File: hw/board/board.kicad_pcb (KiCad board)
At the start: 4 copper layers, 100 x 85 mm, 78 parts, among them J1 Conn_ARM_JTAG_SWD_10, J2 Conn_ARM_JTAG_SWD_10, SW1 TSB008A2526A, SW2 TSB008A2526A, U1 STM32F302CBTx, U2 W25Q128JVSIQTR, U3 AP7361C-18SP-13, U4 AP7361C-10E, U5 TPS54331DR, U6 XC7A35T-FTG256

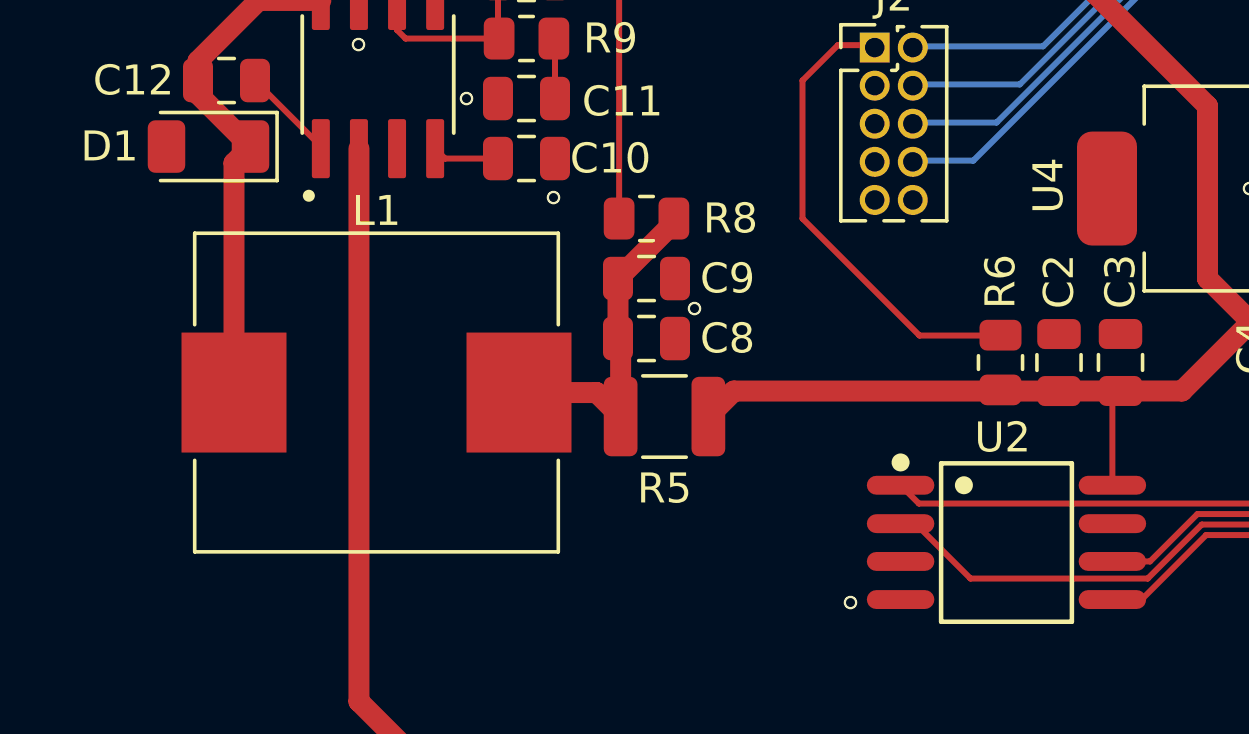
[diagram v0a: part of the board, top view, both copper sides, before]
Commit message: Replaced inductor footprint
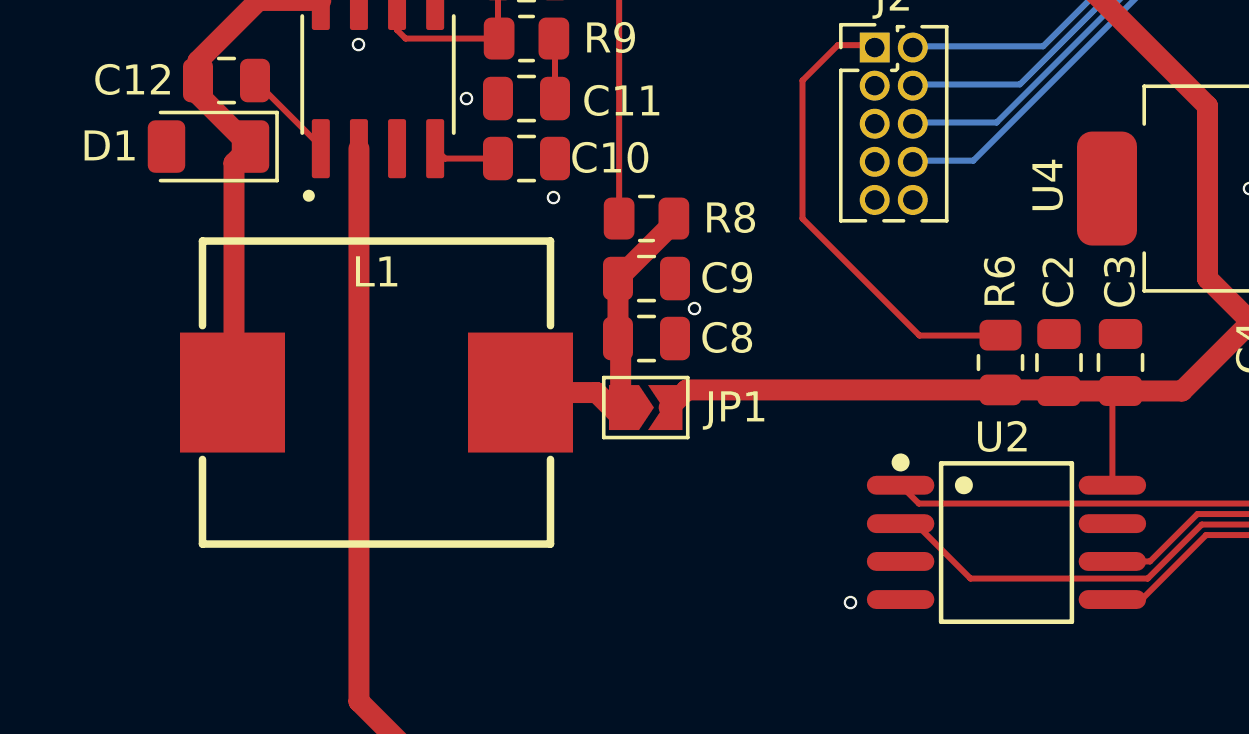
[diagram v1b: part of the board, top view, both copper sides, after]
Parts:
- removed R5: 0, Resistor_SMD:R_1210_3225Metric
- added JP1: SolderJumper_2_Open, Jumper:SolderJumper-2_P1.3mm_Open_TrianglePad1.0x1.5mm, F.Cu at (111.0, 95.5)
- L1: footprint Inductor_SMD:L_Chilisin_BMRF00101040 -> EasyEDA:IND-SMD_L11.6-W10.1
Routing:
- net +2V5: track 241.6 -> 242.8 mm

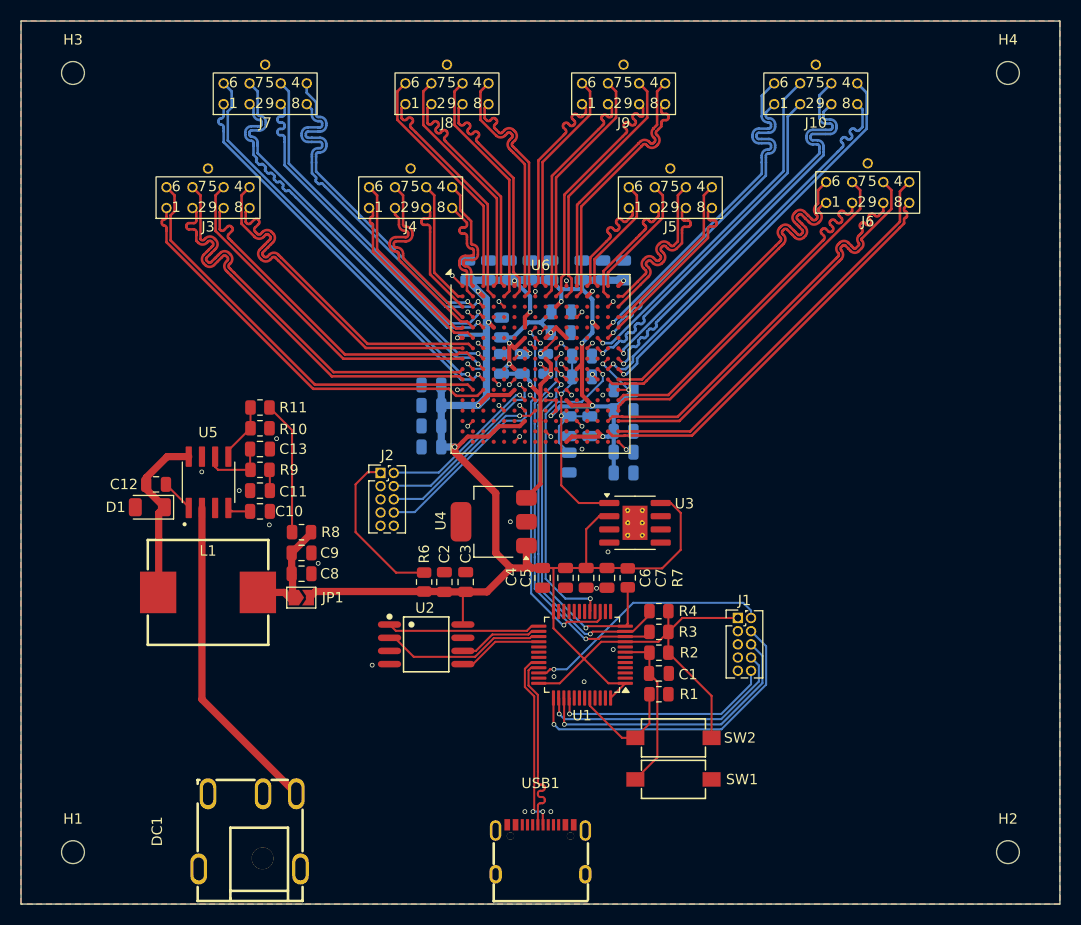
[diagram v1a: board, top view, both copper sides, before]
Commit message: Updated silkscreen
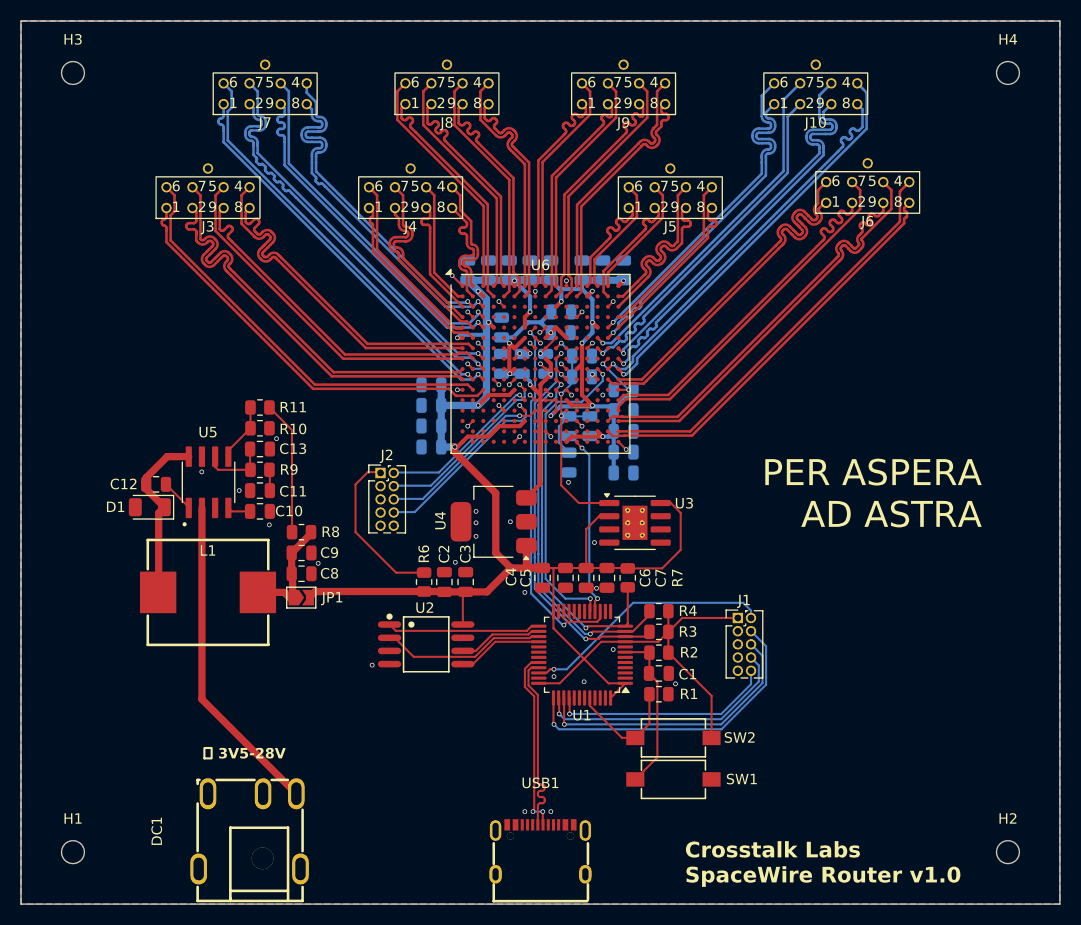
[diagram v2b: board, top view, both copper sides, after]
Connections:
- U1 pad 16: unconnected-(U1-PA6-Pad16) -> DOUT
- U6 pad L15: unconnected-(U6A-IO_L3P_T0_DQS_PUDC_B_14-PadL15) -> GND
- U6 pad T12: unconnected-(U6A-IO_L15N_T2_DQS_DOUT_CSO_B_14-PadT12) -> DOUT
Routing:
- net DOUT: track 0.00 -> 17.3 mm, vias 0 -> 2
- net GND: vias 45 -> 51
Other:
- board text added: "Crosstalk Labs SpaceWire Router v1.0"
- board text added: "PER ASPERA AD ASTRA"
- board text added: "⎓ 3V5-28V"

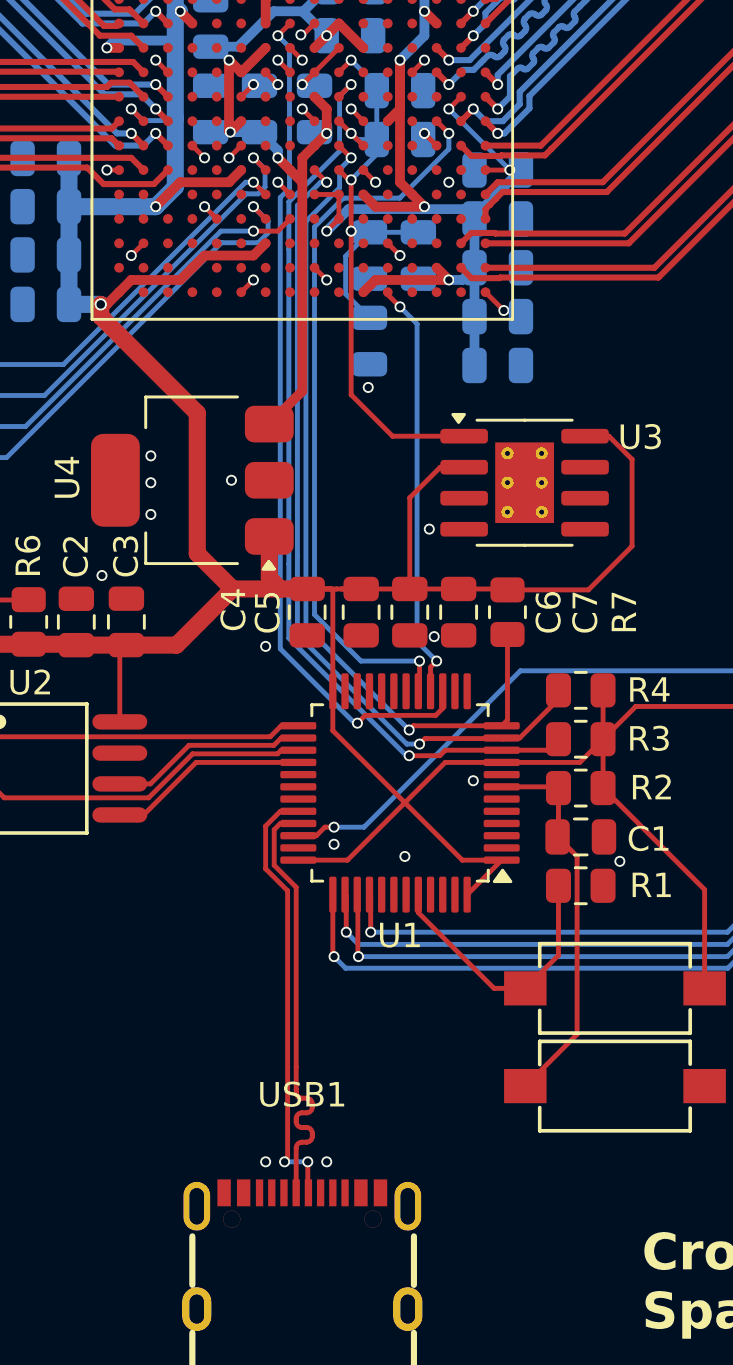
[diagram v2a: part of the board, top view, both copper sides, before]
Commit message: Fixed USB C port
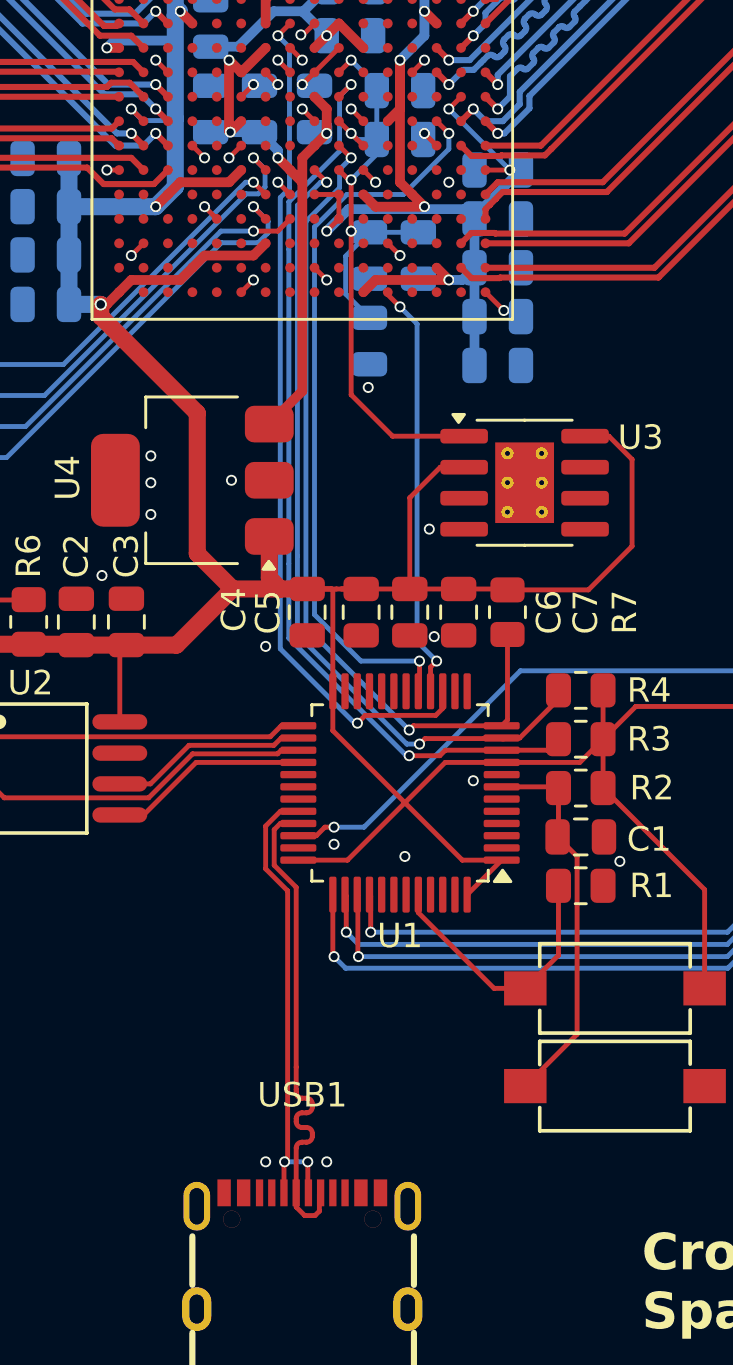
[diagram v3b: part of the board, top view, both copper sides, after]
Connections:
- USB1 pad 5: unconnected-(USB1-DN2-Pad5) -> USB_D_N
- USB1 pad 8: unconnected-(USB1-DP2-Pad8) -> USB_D_P
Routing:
- net USB_D_P: track 18.1 -> 20.6 mm
- net USB_D_N: track 18.0 -> 19.3 mm

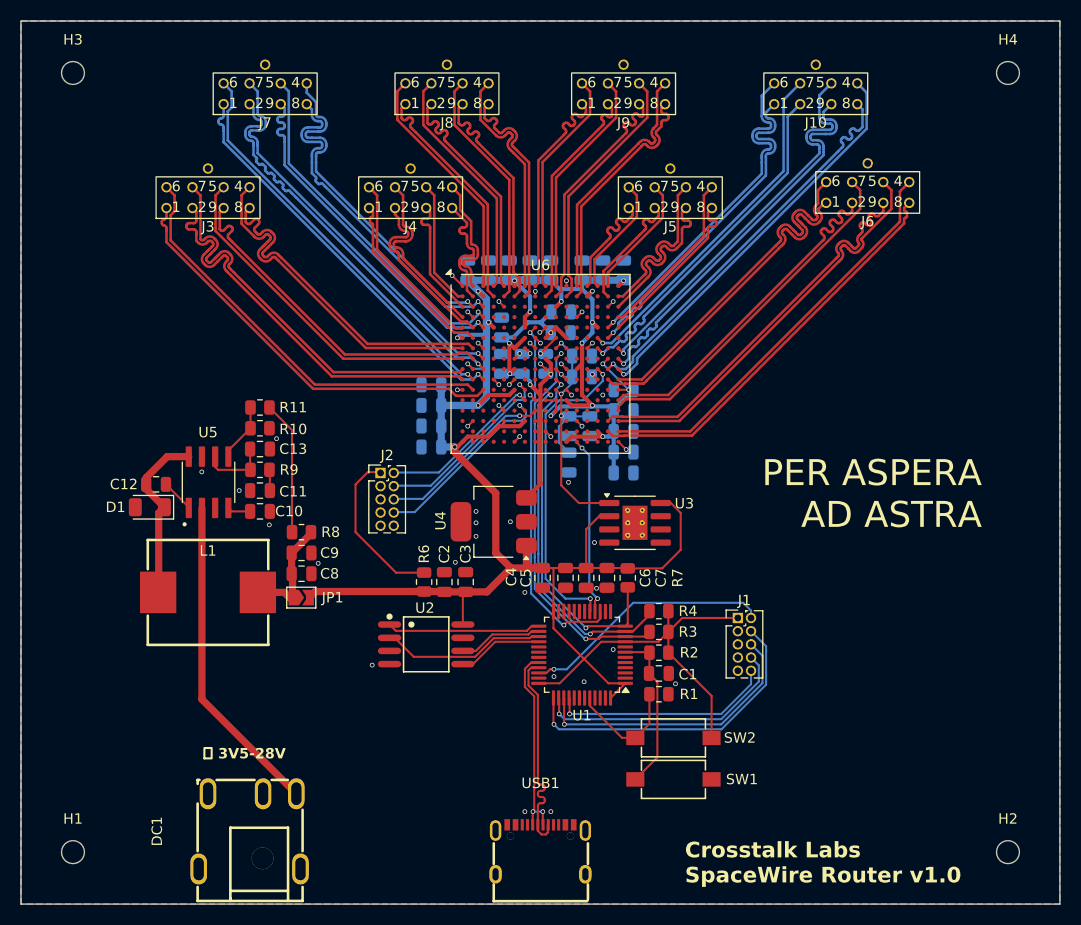
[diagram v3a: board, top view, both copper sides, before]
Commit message: Removed unused 0 ohm resistor, add ground vias
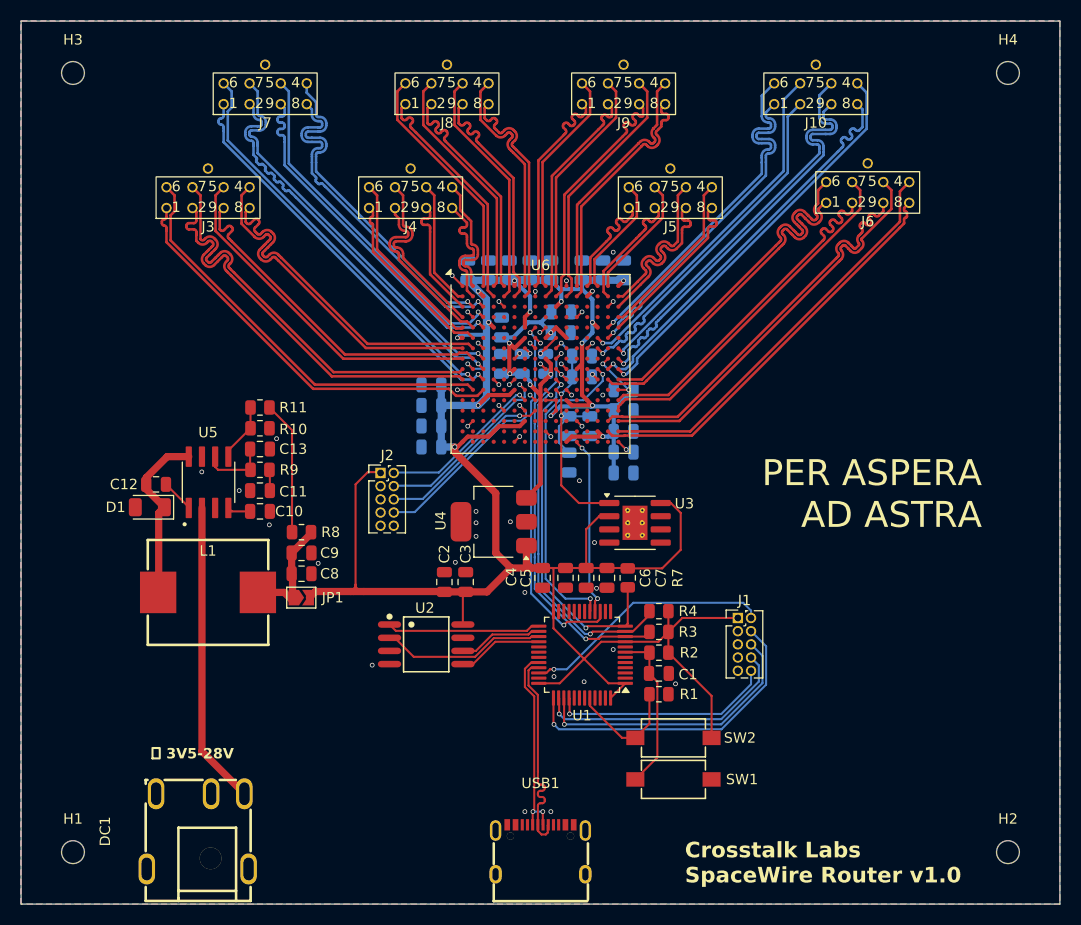
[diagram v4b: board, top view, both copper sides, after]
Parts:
- removed R6: 0, Resistor_SMD:R_0805_2012Metric
- moved DC1 5.00 mm to (101.0, 118.0)
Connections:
- J2 pad 1: Net-(J2-VTref) -> +2V5
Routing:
- net Net-(J2-VTref): track 15.6 -> 0.00 mm
- net +2V5: track 242.8 -> 257.9 mm
- net Net-(U5-VIN): track 31.3 -> 29.2 mm
- net GND: vias 51 -> 52

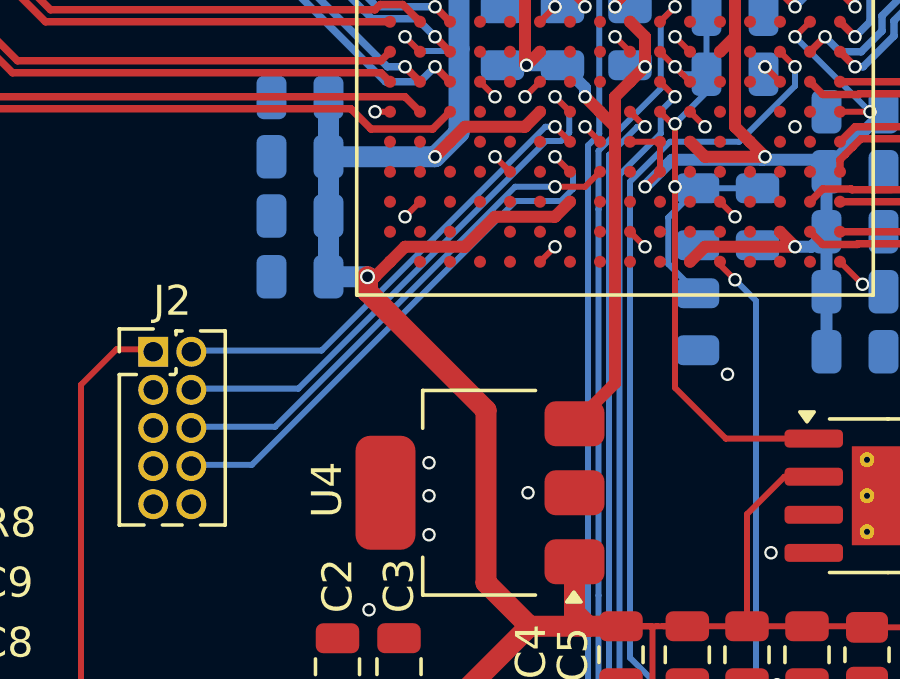
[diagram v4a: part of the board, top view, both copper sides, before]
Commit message: Additional ground stitching vias
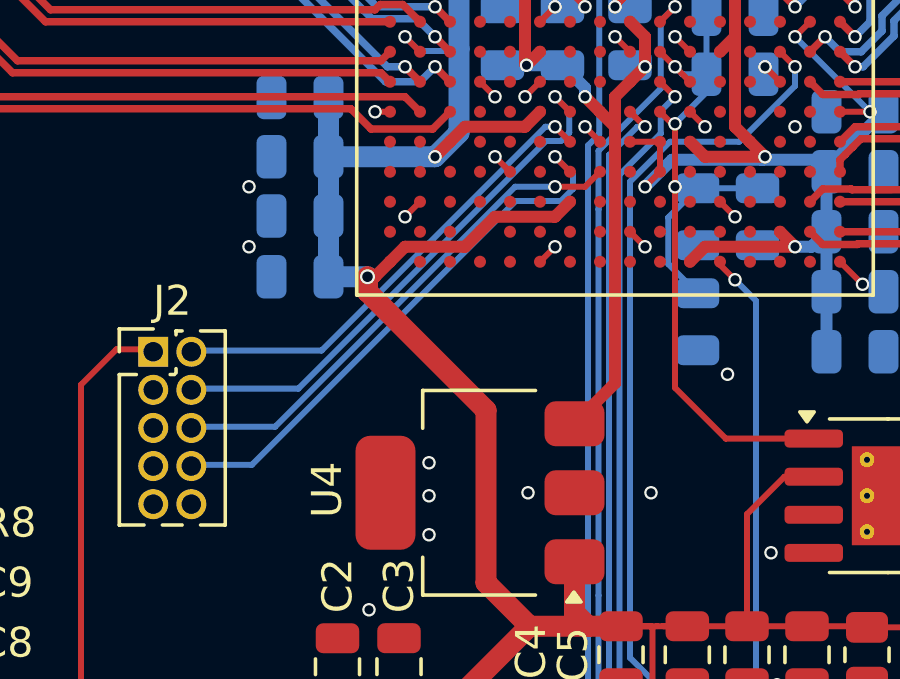
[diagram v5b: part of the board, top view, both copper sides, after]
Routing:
- net GND: vias 52 -> 55
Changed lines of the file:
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@@
 	)
 	(via
+		(at 121.8 80)
+		(size 0.45)
+		(drill 0.3)
+		(layers "F.Cu" "B.Cu")
+		(free yes)
+		(net 5)
+	)
+	(via
 		(at 130 77)
 		(size 0.45)
@@
 	)
 	(via
+		(at 135.2 88.2)
+		(size 0.45)
+		(drill 0.3)
+		(layers "F.Cu" "B.Cu")
+		(free yes)
+		(net 5)
+	)
+	(via
 		(at 135 80)
 		(size 0.45)
@@
 	)
 	(via
+		(at 121.8 78)
+		(size 0.45)
+		(drill 0.3)
+		(layers "F.Cu" "B.Cu")
+		(free yes)
+		(net 5)
+	)
+	(via
 		(at 131.1 88.2)
 		(size 0.45)
@@
 	)
 	(segment
-		(start 138.55 98.25)
-		(end 142.1625 98.25)
+		(start 135.5 74.5)
+		(end 136 75)
 		(width 0.2)
 		(layer "F.Cu")
@@
 	)
 	(segment
-		(start 135.5 74.5)
-		(end 136 75)
+		(start 138.55 98.25)
+		(end 142.1625 98.25)
 		(width 0.2)
 		(layer "F.Cu")
